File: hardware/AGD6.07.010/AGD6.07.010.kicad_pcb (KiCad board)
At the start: 4 copper layers, 90 x 130 mm, 264 parts, among them J1001 PX_ETH GH4, J1002 SIYI_ETH GH4, J1003 CAMF_ETH GH4, J1004 AI_ETH1 GH4, J1005 SERVICE_ETH GH4, J1006 AI_ETH2 GH4, J1007 ETH_SWITCH_MODULE 2x13, J1008 CAMD_ETH GH4, J101 PDB_14S XT30, J202 AI_POWER_12V XT30, J301 PX_CAN1 GH4, J302 PX_CAN2 GH4, J303 PX_TELEM1 SIYI GH6, J304 PX_TELEM2 AI GH6, J305 PX_TELEM3 RADAR GH6, J306 PX_I2C GH4, J307 PX_AD&IO GH8, J308 PX_RC_IN GH3, J309 PX_MAIN 1-8, J310 PX_AUX 1-8, J311 FTS GH3, J312 MODE_SWITCH GH4, J313 LID_BATT_LATCH GH3, J401 ESC1 CAN+PWM GH4, J402 ESC2 CAN+PWM GH4, J403 ESC3 CAN+PWM GH4, J404 ESC4 CAN+PWM GH4, J405 ESC5 CAN+PWM GH4, J406 ESC6 CAN+PWM GH4, J407 PM08-CAN GH4, J408 BMS CAN GH4, J409 REMOTE_ID GH4, J410 GNSS2 (резерв) GH4, J411 OBSTACLE_1 GH4, J412 OBSTACLE_2 GH4, J413 PRESSURE GH3, J414 LEVEL GH3, J415 FLOW GH3, J501 SIYI_PWR XT30, J502 SIYI_DATA GH5, J503 RADAR_US-D1 GH4, J504 GNSS_PPS GH2, J601 AI_SIGNALS GH8, J602 AI_OFF_SWITCH GH2, J603 SERVICE USB-C, J604 AI_USB GH4, J701 TEMP_AI_HEATSINK GH4, J702 TEMP_AIR GH4, J801 VALVE1 XH2, J802 VALVE2 XH2, J803 LIGHTS XH2, J804 FAN XH2, J805 HEATER XH2, J806 PUMP_ESC_SIG GH3, J901 CAM_FRONT_PWR XH2, J902 CAM_DOWN_PWR XH2, J903 CAM_TRIGGER GH3, Q101 100V N-MOSFET >=40A D2PAK (на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, Q201 40V N-MOSFET >=40A D2PAK (нап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, Q801 AO3400A, Q802 AO3401A, Q803 AO3400A, U101 LM5069MM-1, U102 INA228AIDGSR, U201 TPS62133RGTR, U202 AP2112K-3.3TRG1, U203 LM5069MM-2, U204 INA228AIDGSR, U501 TPD4E05U06DQA, U502 TPD4E05U06DQA, U602 TPD4E05U06DQA, U603 USBLC6-2SC6, U701 TPS3430WDRC, U702 TMP117AIDRVR, U703 SHT40-AD1B, U801 BTS5030-1EJA, U802 BTS5030-1EJA, U803 BTS5030-1EJA, U804 ADS1115IDGSR

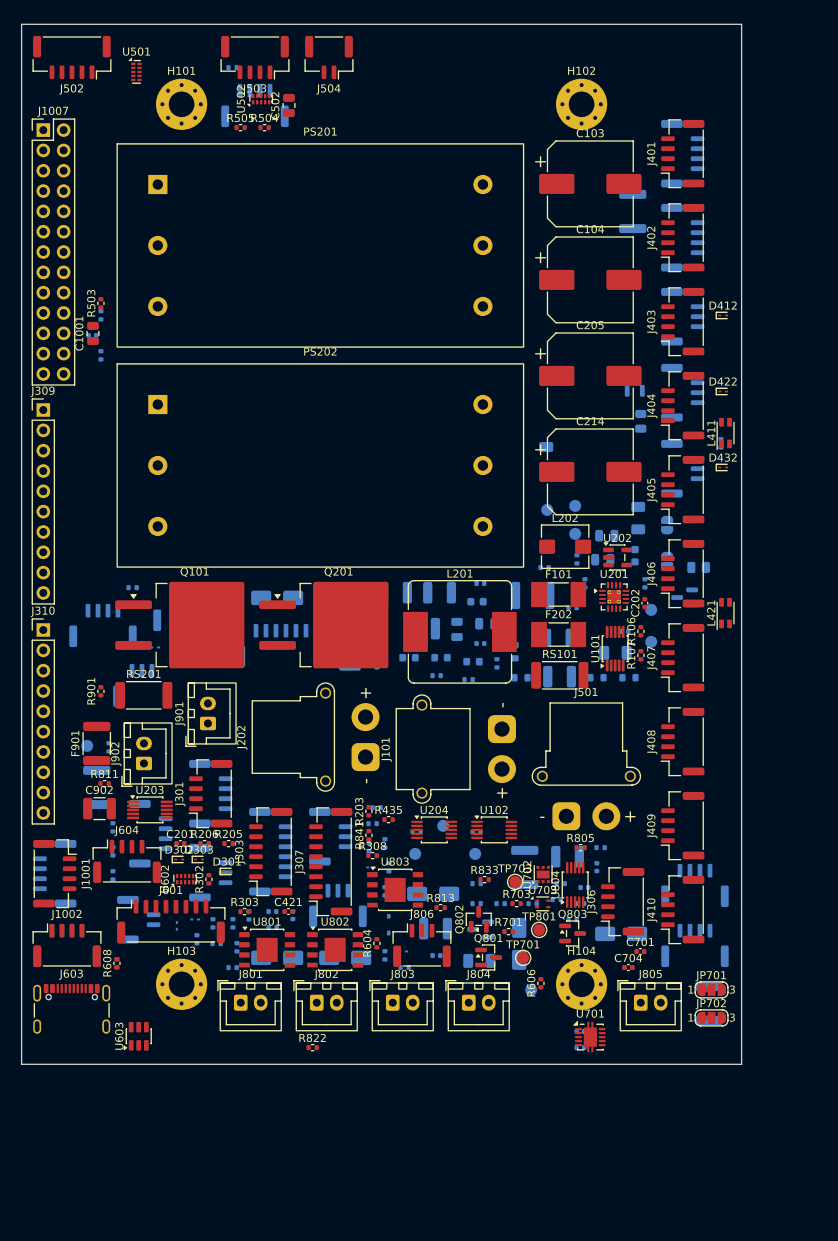
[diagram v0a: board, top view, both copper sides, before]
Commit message: Route AGD6.07.010 board and export fabrication files
Freerouting (10 passes) routed about 94 % of connections on the 90x130
mm 4-layer board; defective autorouter stubs removed. Footprint links
synced with the schematic (library IDs, fields, DNP/BOM flags, NC
pads): schematic parity reports 0 issues and DRC shows no electrical
errors. 32 connections, mostly 14S and AI 12 V power nets, remain for
manual routing as copper pours. Gerber, drill, position and STEP files
exported; status stays NOT_FOR_MANUFACTURE.

Co-Authored-By: Claude Opus 5.5 <noreply@anthropic.com>
Claude-Session: https://claude.ai/code/session_01Qk7uTKdi6YbndB9fGuguYV
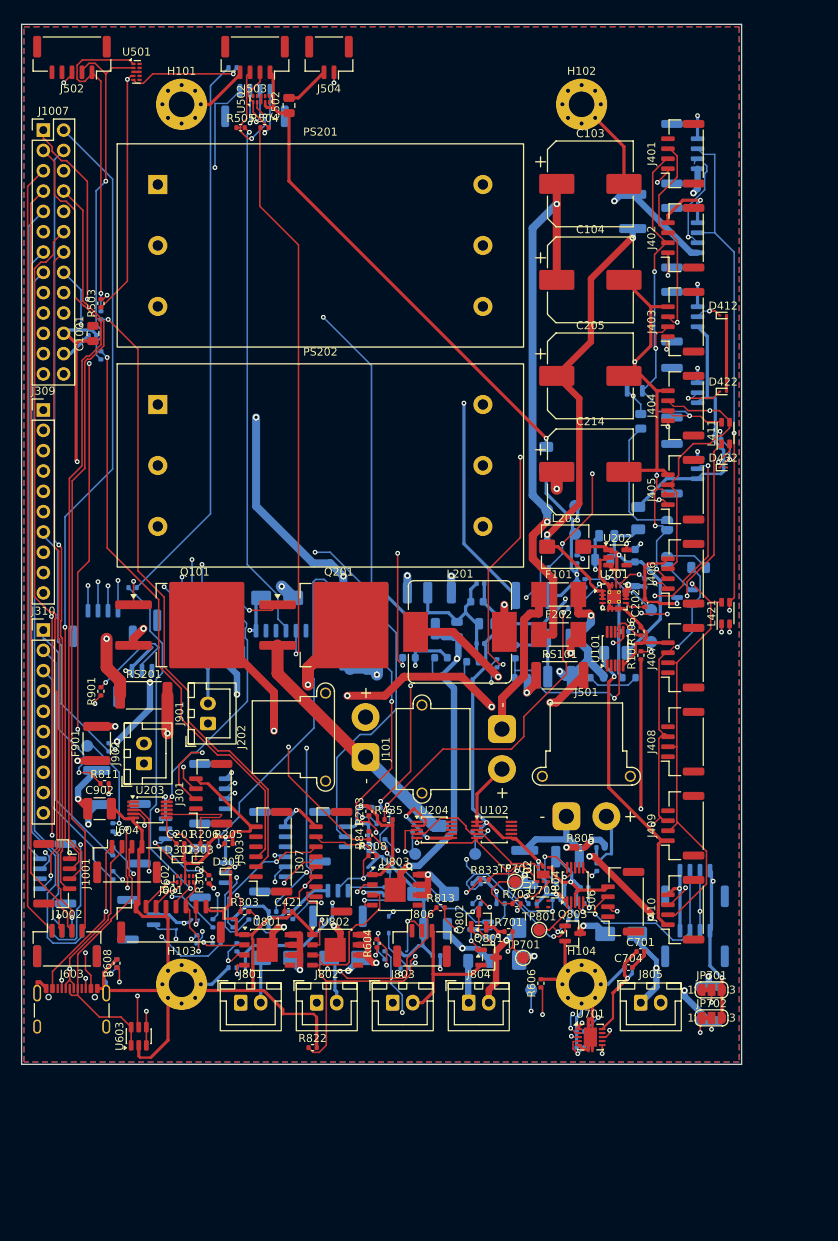
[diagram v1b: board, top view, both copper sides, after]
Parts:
- C1001, C206, C207, C208, C211, C502: footprint C_0805_2012Metric -> Capacitor_SMD:C_0805_2012Metric
- C1002, C101, C106, C201, C202, C215, C411, C421, C431, C701, C702, C703, C704, C705, C804, C811, C821, C831: footprint C_0402_1005Metric -> Capacitor_SMD:C_0402_1005Metric
- C102, C105, C203, C204, C212, C213, C501, C805, C901, C902: footprint C_1210_3225Metric -> Capacitor_SMD:C_1210_3225Metric
- C103, C104, C205, C214: footprint CP_Elec_10x10.5 -> Capacitor_SMD:CP_Elec_10x10.5
- C209, C210: footprint C_0603_1608Metric -> Capacitor_SMD:C_0603_1608Metric
- D101: footprint D_SMB -> Diode_SMD:D_SMB
- D202, D801, D802, D803, D804, D805: footprint D_SMA -> Diode_SMD:D_SMA
- D203: footprint D_SOD-323 -> Diode_SMD:D_SOD-323
- D204, D205, D206: footprint LED_0603_1608Metric -> LED_SMD:LED_0603_1608Metric
- D301, D302, D303, D304, D412, D422, D432, D601, D602, D806, D901: footprint D_SOD-923 -> Diode_SMD:D_SOD-923
- D411, D421, D807, Q801, Q802, Q803: footprint SOT-23 -> Package_TO_SOT_SMD:SOT-23
- F1001, F402, F501, F802, F901, F902: footprint Fuse_1812_4532Metric -> Fuse:Fuse_1812_4532Metric
- F101, F202: footprint Fuse_Littelfuse-NANO2-451_453 -> Fuse:Fuse_Littelfuse-NANO2-451_453
- F401, F403, F502, F801: footprint Fuse_1206_3216Metric -> Fuse:Fuse_1206_3216Metric
- H101, H102, H103, H104: footprint MountingHole_3.2mm_M3_Pad_Via -> MountingHole:MountingHole_3.2mm_M3_Pad_Via
- J1001, J1002, J1003, J1004, J1005, J1006, J1008, J301, J302, J306, J312, J401, J402, J403, J404, J405, J406, J407, J408, J409, J410, J411, J412, J503, J604, J701, J702: footprint JST_GH_SM04B-GHS-TB_1x04-1MP_P1.25mm_Horizontal -> Connector_JST:JST_GH_SM04B-GHS-TB_1x04-1MP_P1.25mm_Horizontal
- J1007: footprint PinHeader_2x13_P2.54mm_Vertical -> Connector_PinHeader_2.54mm:PinHeader_2x13_P2.54mm_Vertical
- J101: footprint AMASS_XT30PW-M_1x02_P2.50mm_Horizontal -> Connector_AMASS:AMASS_XT30PW-M_1x02_P2.50mm_Horizontal
- J202, J501: footprint AMASS_XT30PW-F_1x02_P2.50mm_Horizontal -> Connector_AMASS:AMASS_XT30PW-F_1x02_P2.50mm_Horizontal
- J303, J304, J305: footprint JST_GH_SM06B-GHS-TB_1x06-1MP_P1.25mm_Horizontal -> Connector_JST:JST_GH_SM06B-GHS-TB_1x06-1MP_P1.25mm_Horizontal
- J307, J601: footprint JST_GH_SM08B-GHS-TB_1x08-1MP_P1.25mm_Horizontal -> Connector_JST:JST_GH_SM08B-GHS-TB_1x08-1MP_P1.25mm_Horizontal
- J308, J311, J313, J413, J414, J415, J806, J903: footprint JST_GH_SM03B-GHS-TB_1x03-1MP_P1.25mm_Horizontal -> Connector_JST:JST_GH_SM03B-GHS-TB_1x03-1MP_P1.25mm_Horizontal
- J309, J310: footprint PinHeader_1x10_P2.54mm_Vertical -> Connector_PinHeader_2.54mm:PinHeader_1x10_P2.54mm_Vertical
- J502: footprint JST_GH_SM05B-GHS-TB_1x05-1MP_P1.25mm_Horizontal -> Connector_JST:JST_GH_SM05B-GHS-TB_1x05-1MP_P1.25mm_Horizontal
- J504, J602: footprint JST_GH_SM02B-GHS-TB_1x02-1MP_P1.25mm_Horizontal -> Connector_JST:JST_GH_SM02B-GHS-TB_1x02-1MP_P1.25mm_Horizontal
- J603: footprint USB_C_Receptacle_GCT_USB4105-xx-A_16P_TopMnt_Horizontal -> Connector_USB:USB_C_Receptacle_GCT_USB4105-xx-A_16P_TopMnt_Horizontal
- J801, J802, J803, J804, J805, J901, J902: footprint JST_XH_B2B-XH-A_1x02_P2.50mm_Vertical -> Connector_JST:JST_XH_B2B-XH-A_1x02_P2.50mm_Vertical
- JP411, JP421: footprint SolderJumper-2_P1.3mm_Open_RoundedPad1.0x1.5mm -> Jumper:SolderJumper-2_P1.3mm_Open_RoundedPad1.0x1.5mm
- JP701, JP702: footprint SolderJumper-3_P1.3mm_Bridged12_RoundedPad1.0x1.5mm_NumberLabels -> Jumper:SolderJumper-3_P1.3mm_Bridged12_RoundedPad1.0x1.5mm_NumberLabels
- L201: footprint L_Bourns_SRP1245A -> Inductor_SMD:L_Bourns_SRP1245A
- L202: footprint L_Bourns_SRP5030T -> Inductor_SMD:L_Bourns_SRP5030T
- L411, L421: footprint L_CommonMode_Wurth_WE-CNSW-1206 -> Inductor_SMD:L_CommonMode_Wurth_WE-CNSW-1206
- PS201, PS202: footprint DCDC_2x1in_PLACEHOLDER -> AGD6:DCDC_2x1in_PLACEHOLDER
- Q101, Q201: footprint TO-263-2 -> Package_TO_SOT_SMD:TO-263-2
- R101, R106, R107, R108, R201, R202, R203, R204, R205, R206, R207, R208, R209, R210, R211, R212, R213, R301, R302, R303, R304, R305, R306, R307, R308, R309, R310, R311, R413, R414, R423, R424, R433, R434, R435, R501, R502, R503, R504, R505, R506, R601, R602, R603, R604, R605, R606, R607, R608, R609, R701, R702, R703, R804, R805, R806, R807, R811, R812, R813, R821, R822, R823, R831, R832, R833, R841, R842, R851, R852, R861, R901: footprint R_0402_1005Metric -> Resistor_SMD:R_0402_1005Metric
- R102, R103, R104, R105: footprint R_0603_1608Metric -> Resistor_SMD:R_0603_1608Metric
- R411, R421: footprint R_0805_2012Metric -> Resistor_SMD:R_0805_2012Metric
- RS101, RS201: footprint R_2512_6332Metric -> Resistor_SMD:R_2512_6332Metric
- TP101, TP102, TP103, TP201, TP202, TP203, TP204, TP205, TP206, TP207, TP701, TP702, TP703, TP801: footprint TestPoint_Pad_D1.5mm -> TestPoint:TestPoint_Pad_D1.5mm
- U101, U203: footprint MSOP-10_3x3mm_P0.5mm -> Package_SO:MSOP-10_3x3mm_P0.5mm
- U102, U204, U804: footprint TSSOP-10_3x3mm_P0.5mm -> Package_SO:TSSOP-10_3x3mm_P0.5mm
- U201: footprint VQFN-16-1EP_3x3mm_P0.5mm_EP1.68x1.68mm_ThermalVias -> Package_DFN_QFN:VQFN-16-1EP_3x3mm_P0.5mm_EP1.68x1.68mm_ThermalVias
- U202: footprint SOT-23-5 -> Package_TO_SOT_SMD:SOT-23-5
- U501, U502, U602: footprint USON-10_2.5x1.0mm_P0.5mm -> Package_SON:USON-10_2.5x1.0mm_P0.5mm
- U603: footprint SOT-23-6 -> Package_TO_SOT_SMD:SOT-23-6
- U701: footprint VSON-10-1EP_3x3mm_P0.5mm_EP1.65x2.4mm -> Package_SON:VSON-10-1EP_3x3mm_P0.5mm_EP1.65x2.4mm
- U702: footprint WSON-6-1EP_2x2mm_P0.65mm_EP1x1.6mm -> Package_SON:WSON-6-1EP_2x2mm_P0.65mm_EP1x1.6mm
- U703: footprint Sensirion_DFN-4_1.5x1.5mm_P0.8mm_SHT4x_NoCentralPad -> Sensor_Humidity:Sensirion_DFN-4_1.5x1.5mm_P0.8mm_SHT4x_NoCentralPad
- U801, U802, U803: footprint Infineon_PG-DSO-8-43 -> Package_SO:Infineon_PG-DSO-8-43
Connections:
- J301 pad 1: unconnected-(J301-Pin_1-Pad1) -> (no net)
- J302 pad 1: unconnected-(J302-Pin_1-Pad1) -> (no net)
- J303 pad 1: unconnected-(J303-Pin_1-Pad1) -> (no net)
- J303 pad 4: unconnected-(J303-Pin_4-Pad4) -> (no net)
- J303 pad 5: unconnected-(J303-Pin_5-Pad5) -> (no net)
- J304 pad 1: unconnected-(J304-Pin_1-Pad1) -> (no net)
- J304 pad 4: unconnected-(J304-Pin_4-Pad4) -> (no net)
- J304 pad 5: unconnected-(J304-Pin_5-Pad5) -> (no net)
- J305 pad 1: unconnected-(J305-Pin_1-Pad1) -> (no net)
- J305 pad 4: unconnected-(J305-Pin_4-Pad4) -> (no net)
- J305 pad 5: unconnected-(J305-Pin_5-Pad5) -> (no net)
- J306 pad 1: unconnected-(J306-Pin_1-Pad1) -> (no net)
- J307 pad 1: unconnected-(J307-Pin_1-Pad1) -> (no net)
- J308 pad 1: unconnected-(J308-Pin_1-Pad1) -> (no net)
- J309 pad 8: unconnected-(J309-Pin_8-Pad8) -> (no net)
- J310 pad 8: unconnected-(J310-Pin_8-Pad8) -> (no net)
- J311 pad 1: unconnected-(J311-Pin_1-Pad1) -> (no net)
- J407 pad 1: unconnected-(J407-Pin_1-Pad1) -> (no net)
- J408 pad 1: unconnected-(J408-Pin_1-Pad1) -> (no net)
- J502 pad 5: unconnected-(J502-Pin_5-Pad5) -> (no net)
- J603 pad A8: unconnected-(J603-SBU1-PadA8) -> (no net)
- J603 pad B8: unconnected-(J603-SBU2-PadB8) -> (no net)
- J806 pad 1: unconnected-(J806-Pin_1-Pad1) -> (no net)
- J903 pad 1: unconnected-(J903-Pin_1-Pad1) -> (no net)
- PS201 pad 3: unconnected-(PS201-ON/OFF-Pad3) -> (no net)
- PS201 pad 5: unconnected-(PS201-TRIM-Pad5) -> (no net)
- PS202 pad 3: unconnected-(PS202-ON/OFF-Pad3) -> (no net)
- PS202 pad 5: unconnected-(PS202-TRIM-Pad5) -> (no net)
- U202 pad 4: unconnected-(U202-NC-Pad4) -> (no net)
- U501 pad 10: unconnected-(U501-NC-Pad10) -> (no net)
- U501 pad 6: unconnected-(U501-NC-Pad6) -> (no net)
- U501 pad 7: unconnected-(U501-NC-Pad7) -> (no net)
- U501 pad 9: unconnected-(U501-NC-Pad9) -> (no net)
- U502 pad 10: unconnected-(U502-NC-Pad10) -> (no net)
- U502 pad 5: unconnected-(U502-D2--Pad5) -> (no net)
- U502 pad 6: unconnected-(U502-NC-Pad6) -> (no net)
- U502 pad 7: unconnected-(U502-NC-Pad7) -> (no net)
- U502 pad 9: unconnected-(U502-NC-Pad9) -> (no net)
- U602 pad 10: unconnected-(U602-NC-Pad10) -> (no net)
- U602 pad 6: unconnected-(U602-NC-Pad6) -> (no net)
- U602 pad 7: unconnected-(U602-NC-Pad7) -> (no net)
- U602 pad 9: unconnected-(U602-NC-Pad9) -> (no net)
- U701 pad 9: unconnected-(U701-NC-Pad9) -> (no net)
- U801 pad 5: unconnected-(U801-NC-Pad5) -> (no net)
- U802 pad 5: unconnected-(U802-NC-Pad5) -> (no net)
- U803 pad 5: unconnected-(U803-NC-Pad5) -> (no net)
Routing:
- net GND: track 0.00 -> 555.4 mm, vias 0 -> 23
- net +12V: track 0.00 -> 347.7 mm, vias 0 -> 17
- net +3V3: track 0.00 -> 321.3 mm, vias 0 -> 20
- net /VIN_PROT: track 0.00 -> 219.8 mm, vias 0 -> 5
- net /CAN_AND_SENSORS/C2L: track 0.00 -> 122.0 mm, vias 0 -> 5
- net /CAN_AND_SENSORS/C2H: track 0.00 -> 117.9 mm, vias 0 -> 2
- net /POWER_CONVERSION/V12_AI: track 0.00 -> 113.7 mm, vias 0 -> 1
- net /CAN1_L: track 0.00 -> 105.6 mm, vias 0 -> 2
- net /ETHERNET/V5_ETH: track 0.00 -> 104.4 mm, vias 0 -> 2
- net /SBUS: track 0.00 -> 102.4 mm, vias 0 -> 2
- net /ESC_PWM6: track 0.00 -> 99.2 mm, vias 0 -> 1
- net /ETHERNET/E2_TXN: track 0.00 -> 98.9 mm, vias 0 -> 1
- net /CAN1_H: track 0.00 -> 98.8 mm, vias 0 -> 4
- net /ETHERNET/E1_TXP: track 0.00 -> 98.7 mm, vias 0 -> 4
- net /ETHERNET/E1_TXN: track 0.00 -> 98.7 mm, vias 0 -> 1
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- added copper zone on B.Cu, net GND
- added copper zone on F.Cu, net GND

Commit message: AGD6.07.010 rev 0.3: design review fixes and bring-up plan
Design review (DESIGN_REVIEW.md) with fixes applied to the schematic:
INA228 input RC filters, 12 V bus current monitor (INA228 0x45),
BTS5030 diagnostic scaling with clamp diodes, flow input level fix,
CAN1 changed from star to daisy chain with on-board terminator, AI
shutdown request, board buzzer, series resistors and ESD on external
I2C probes. Connectors merged so every connector sits on a board edge.
Adds calculations.md (power, IPC-2221 widths, hot-swap, thermal, ADC
scaling, CAN, clearances) and BRINGUP.md (step-by-step test plan).
ERC: no errors; all 820 intended pin connections verified. Board is
re-placed; routing in progress.

Co-Authored-By: Claude Opus 5.5 <noreply@anthropic.com>
Claude-Session: https://claude.ai/code/session_01Qk7uTKdi6YbndB9fGuguYV
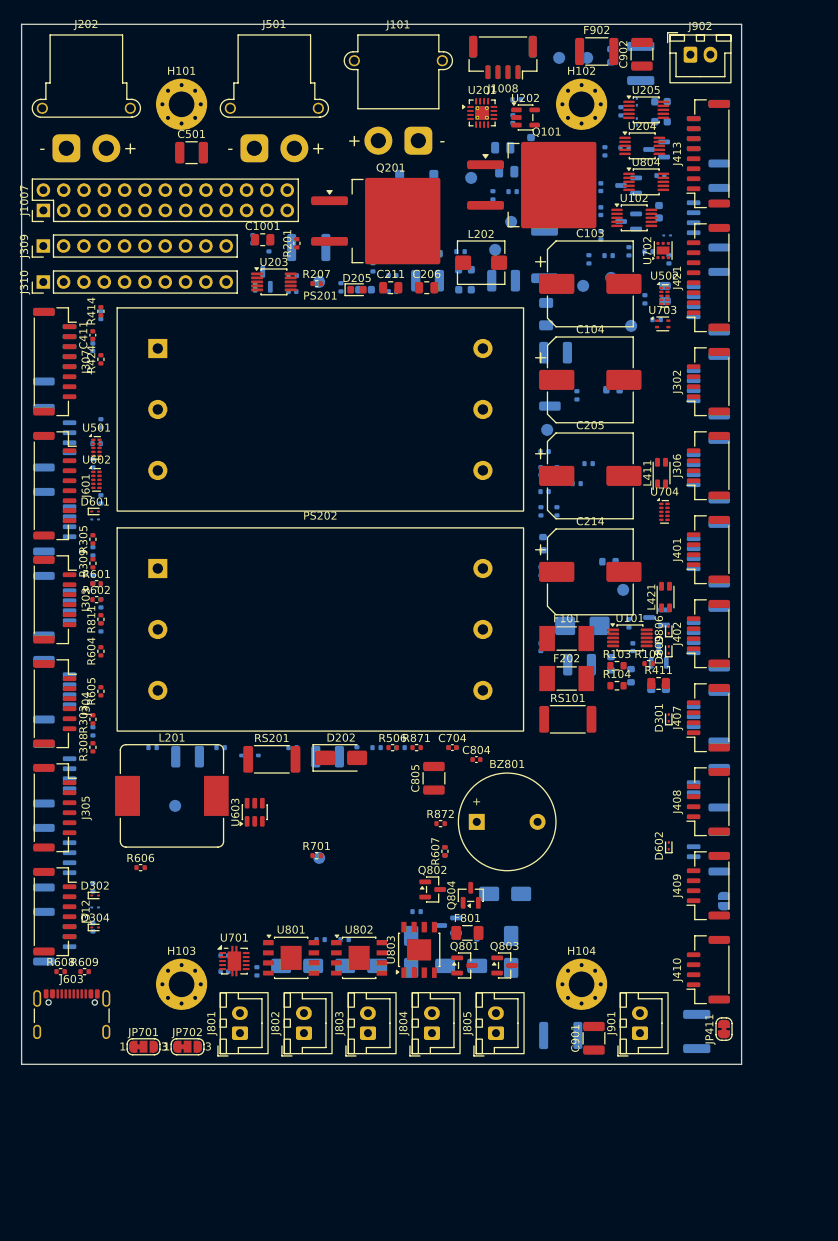
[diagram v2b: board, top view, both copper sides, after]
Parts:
- removed D901: ESD9B5.0ST5G, Diode_SMD:D_SOD-923
- removed J313: LID_BATT_LATCH GH3, Connector_JST:JST_GH_SM03B-GHS-TB_1x03-1MP_P1.25mm_Horizontal
- removed J403: ESC3 CAN+PWM GH4, Connector_JST:JST_GH_SM04B-GHS-TB_1x04-1MP_P1.25mm_Horizontal
- removed J404: ESC4 CAN+PWM GH4, Connector_JST:JST_GH_SM04B-GHS-TB_1x04-1MP_P1.25mm_Horizontal
- removed J405: ESC5 CAN+PWM GH4, Connector_JST:JST_GH_SM04B-GHS-TB_1x04-1MP_P1.25mm_Horizontal
- removed J406: ESC6 CAN+PWM GH4, Connector_JST:JST_GH_SM04B-GHS-TB_1x04-1MP_P1.25mm_Horizontal
- removed J414: LEVEL GH3, Connector_JST:JST_GH_SM03B-GHS-TB_1x03-1MP_P1.25mm_Horizontal
- removed J415: FLOW GH3, Connector_JST:JST_GH_SM03B-GHS-TB_1x03-1MP_P1.25mm_Horizontal
- removed J903: CAM_TRIGGER GH3, Connector_JST:JST_GH_SM03B-GHS-TB_1x03-1MP_P1.25mm_Horizontal
- removed R901: 100, Resistor_SMD:R_0402_1005Metric
- added BZ801: 12V active buzzer, Buzzer_Beeper:Buzzer_12x9.5RM7.6, F.Cu at (156.9, 149.7)
- added C107: 100n 100V, Capacitor_SMD:C_0603_1608Metric, B.Cu at (179.7, 73.4)
- added C216: 100n, Capacitor_SMD:C_0603_1608Metric, B.Cu at (179.9, 62.2)
- added C217: 100n, Capacitor_SMD:C_0603_1608Metric, B.Cu at (179.9, 59.7)
- added C218: 22u 25V, Capacitor_SMD:C_1210_3225Metric, B.Cu at (160.2, 82.0)
- added C219: 100n, Capacitor_SMD:C_0402_1005Metric, B.Cu at (146.4, 81.4)
- added D433: BAT54S, Package_TO_SOT_SMD:SOT-23, B.Cu at (130.1, 81.9)
- added D603: ESD9B5.0ST5G, Diode_SMD:D_SOD-923, B.Cu at (109.2, 111.9)
- added D808: SS14, Diode_SMD:D_SMA, B.Cu at (160.4, 158.7)
- added D809: ESD9B5.0ST5G, Diode_SMD:D_SOD-923, F.Cu at (180.9, 128.2)
- added D811: BAT54S, Package_TO_SOT_SMD:SOT-23, B.Cu at (175.9, 70.1)
- added D812: BAT54S, Package_TO_SOT_SMD:SOT-23, B.Cu at (175.9, 74.6)
- added D813: BAT54S, Package_TO_SOT_SMD:SOT-23, B.Cu at (179.4, 65.6)
- added J421: ESC1-6 PWM backup GH8, Connector_JST:JST_GH_SM08B-GHS-TB_1x08-1MP_P1.25mm_Horizontal, F.Cu at (185.9, 81.7)
- added Q804: AO3400A, Package_TO_SOT_SMD:SOT-23, F.Cu at (156.1, 158.9)
- added R109: 10, Resistor_SMD:R_0603_1608Metric, B.Cu at (173.4, 117.2)
- added R110: 10, Resistor_SMD:R_0603_1608Metric, B.Cu at (173.9, 95.7)
- added R214: 10, Resistor_SMD:R_0603_1608Metric, B.Cu at (165.2, 114.9)
- added R215: 10, Resistor_SMD:R_0603_1608Metric, B.Cu at (151.4, 78.7)
- added R216: 10, Resistor_SMD:R_0603_1608Metric, B.Cu at (170.2, 72.9)
- added R217: 10, Resistor_SMD:R_0603_1608Metric, B.Cu at (173.7, 53.9)
- added R218: 10k, Resistor_SMD:R_0402_1005Metric, B.Cu at (174.9, 60.9)
- added R610: 100, Resistor_SMD:R_0402_1005Metric, B.Cu at (109.9, 99.9)
- added R704: 33, Resistor_SMD:R_0402_1005Metric, B.Cu at (179.4, 86.9)
- added R705: 33, Resistor_SMD:R_0402_1005Metric, B.Cu at (177.9, 84.4)
- added R862: 100, Resistor_SMD:R_0402_1005Metric, B.Cu at (166.9, 118.4)
- added R871: 100, Resistor_SMD:R_0402_1005Metric, F.Cu at (149.4, 140.4)
- added R872: 100k, Resistor_SMD:R_0402_1005Metric, F.Cu at (152.4, 149.9)
- added RS202: 10m 1W, Resistor_SMD:R_2512_6332Metric, B.Cu at (165.4, 78.8)
- added TP208: V12_ALERT_N, TestPoint:TestPoint_Pad_D1.5mm, B.Cu at (167.2, 54.2)
- added U205: INA228AIDGSR, Package_SO:TSSOP-10_3x3mm_P0.5mm, F.Cu at (178.1, 60.7)
- added U704: TPD4E05U06DQA, Package_SON:USON-10_2.5x1.0mm_P0.5mm, F.Cu at (180.4, 110.9)
- C201, C202, C421, C502, C701, D303, D412, D422, D432, F901, J1001, J1002, J301, J502, J503, J504, J604, R107, R203, R205, R206, R302, R503, R504, R505, R703, R805, R813, R833, R841, TP701, TP703, TP801: moved to B.Cu
- C206, C211, C411, C501, C804, C805, C901, D202, D205, D304, D601, D602, D806, F801, F902, J1008, J302, J304, J305, R103, R104, R201, R207, R305, R309, R411, R414, R424, R506, R601, R602, R605, R607, R609: moved to F.Cu
- J312: value MODE_SWITCH GH4 -> MODE_SWITCH + LID/BATT_LATCH GH6; footprint Connector_JST:JST_GH_SM04B-GHS-TB_1x04-1MP_P1.25mm_Horizontal -> Connector_JST:JST_GH_SM06B-GHS-TB_1x06-1MP_P1.25mm_Horizontal; moved to F.Cu
- J401: value ESC1 CAN+PWM GH4 -> CAN1 ESC CHAIN START GH4
- J402: value ESC2 CAN+PWM GH4 -> CAN1 ESC CHAIN RETURN GH4
- J413: value PRESSURE GH3 -> SPRAY_SENSORS GH8 (давл./уровень/расход); footprint Connector_JST:JST_GH_SM03B-GHS-TB_1x03-1MP_P1.25mm_Horizontal -> Connector_JST:JST_GH_SM08B-GHS-TB_1x08-1MP_P1.25mm_Horizontal; moved to F.Cu
- J806: value PUMP_ESC_SIG GH3 -> PUMP_PWM + CAM_TRIG GH4; footprint Connector_JST:JST_GH_SM03B-GHS-TB_1x03-1MP_P1.25mm_Horizontal -> Connector_JST:JST_GH_SM04B-GHS-TB_1x04-1MP_P1.25mm_Horizontal; moved to B.Cu
- JP411: value TERM_CAN1 -> TERM_CAN1 (замкнута); footprint Jumper:SolderJumper-2_P1.3mm_Open_RoundedPad1.0x1.5mm -> Jumper:SolderJumper-2_P1.3mm_Bridged_RoundedPad1.0x1.5mm; moved to F.Cu
- R435: value 20k -> 33k; moved to B.Cu
- R812, R832: value 1.2k -> 470
- R822: value 1.2k -> 470; moved to B.Cu
- moved C902 116.1 mm to (177.5, 53.7), turned to 90 degrees
- moved J902 111.9 mm to (183.6, 53.8), turned to 0 degrees
- moved F902 111.2 mm to (171.9, 53.4), turned to 0 degrees
- moved J504 102.9 mm to (185.9, 145.4), turned to -90 degrees
- moved TP206 101.8 mm to (170.7, 54.2)
- moved C501 99.8 mm to (121.2, 66.0), turned to 0 degrees
- moved J301 99.0 mm to (160.2, 54.1), turned to 0 degrees
- moved R807 94.6 mm to (170.9, 67.4), turned to 90 degrees
- moved J604 93.9 mm to (185.9, 95.2), turned to -90 degrees
- moved J501 92.2 mm to (129.1, 65.5)
- moved C811 89.6 mm to (172.4, 70.4), turned to 90 degrees
- moved U204 89.4 mm to (177.6, 65.2)
- moved R208 89.4 mm to (175.4, 65.4)
- moved U804 88.3 mm to (178.1, 69.7), turned to 0 degrees
- moved R506 87.3 mm to (146.4, 140.4), turned to 0 degrees
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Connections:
- J309 pad 8: (no net) -> /AI_SHDN_REQ
- J310 pad 8: (no net) -> /BUZZER_CTL
- J312 pad 4: GND -> /FLIGHT_CONTROL_IO/ENCL_COM
- J401 pad 1: /ESC_PWM1 -> (no net)
- J402 pad 1: /ESC_PWM2 -> (no net)
- J413 pad 3: GND -> /CAN_AND_SENSORS/LEVEL_IN
- J601 pad 8: GND -> /AI_COMPUTE_INTERFACE/SHDN_C
- J701 pad 2: /I2C_SCL -> /WATCHDOG_DIAGNOSTICS/P_SCL
- J701 pad 3: /I2C_SDA -> /WATCHDOG_DIAGNOSTICS/P_SDA
- J702 pad 2: /I2C_SCL -> /WATCHDOG_DIAGNOSTICS/P_SCL
- J702 pad 3: /I2C_SDA -> /WATCHDOG_DIAGNOSTICS/P_SDA
- J806 pad 1: (no net) -> /LOAD_SWITCHES_12V/PUMP_C
- J806 pad 2: /LOAD_SWITCHES_12V/PUMP_C -> /LOAD_SWITCHES_12V/TRIG_C
- PS201 pad 4: +12V -> /POWER_CONVERSION/V12_RAW
- U102 pad 10: /POWER_INPUT_14S/VIN_F -> /POWER_INPUT_14S/INA1_P
- U102 pad 9: /POWER_INPUT_14S/SNS -> /POWER_INPUT_14S/INA1_N
- U204 pad 10: /POWER_CONVERSION/V12AI_RAW -> /POWER_CONVERSION/INA2_P
- U204 pad 9: /POWER_CONVERSION/AI_SNS -> /POWER_CONVERSION/INA2_N
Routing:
- net GND: track 555.4 -> 0.00 mm, vias 23 -> 0
- net +12V: track 347.7 -> 0.00 mm, vias 17 -> 0
- net +3V3: track 321.3 -> 0.00 mm, vias 20 -> 0
- net /VIN_PROT: track 219.8 -> 0.00 mm, vias 5 -> 0
- net /CAN_AND_SENSORS/C2L: track 122.0 -> 0.00 mm, vias 5 -> 0
- net /CAN_AND_SENSORS/C2H: track 117.9 -> 0.00 mm, vias 2 -> 0
- net /POWER_CONVERSION/V12_AI: track 113.7 -> 0.00 mm, vias 1 -> 0
- net /CAN1_L: track 105.6 -> 0.00 mm, vias 2 -> 0
- net /ETHERNET/V5_ETH: track 104.4 -> 0.00 mm, vias 2 -> 0
- net /SBUS: track 102.4 -> 0.00 mm, vias 2 -> 0
- net /ESC_PWM6: track 99.2 -> 0.00 mm, vias 1 -> 0
- net /ETHERNET/E2_TXN: track 98.9 -> 0.00 mm, vias 1 -> 0
- net /CAN1_H: track 98.8 -> 0.00 mm, vias 4 -> 0
- net /ETHERNET/E1_TXP: track 98.7 -> 0.00 mm, vias 4 -> 0
- net /ETHERNET/E1_TXN: track 98.7 -> 0.00 mm, vias 1 -> 0
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- removed copper zone on B.Cu, net GND
- removed copper zone on F.Cu, net GND
